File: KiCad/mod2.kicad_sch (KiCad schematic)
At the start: 49 parts, among them M3 Fan_4pin, M4 Fan_4pin, U2 ZD25Q64BSIGT

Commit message: Copy modules 2 and 3, remove unnecessary pages
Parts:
- removed D6: B0520W, Diode_SMD:D_SOD-123, symbol Device:D_Schottky
- removed D7, D8: LED, LED_SMD:LED_0603_1608Metric, symbol Device:LED
- removed R40, R41: 10k, Resistor_SMD:R_0402_1005Metric, symbol Device:R_Small
- removed U2: ZD25Q64BSIGT, Package_SO:SOIC-8_5.3x5.3mm_P1.27mm, symbol Memory_Flash:W25Q128JVS
- added C21, C22, C23, C24, C25, C26: 100nF, Capacitor_SMD:C_0402_1005Metric, symbol Device:C_Small
- added C27, C28, C29, C30, C31, C32, C33, C366, C367: 220nF, Capacitor_SMD:C_0402_1005Metric, symbol Device:C_Small
- added C368, C372, C373, C376: 100nF/50V, Capacitor_SMD:C_0402_1005Metric, symbol Device:C
- added C369: 10uF/10V, Capacitor_SMD:C_0603_1608Metric, symbol Device:C
- added C370, C378: 27pF, Capacitor_SMD:C_0402_1005Metric, symbol Device:C_Small
- added C371: 390pF, Capacitor_SMD:C_0402_1005Metric, symbol Device:C
- added C374, C375: 100uF/25V, Capacitor_SMD:CP_Elec_6.3x7.7, symbol Device:C_Polarized
- added C377: 560uF/25V, Capacitor_SMD:CP_Elec_6.3x7.7, symbol Device:C_Polarized
- added C379: 100pF, Capacitor_SMD:C_0402_1005Metric, symbol Device:C_Small
- added D4, D7: B0520W, Diode_SMD:D_SOD-123, symbol Device:D_Schottky
- added D6: LED, LED_SMD:LED_0603_1608Metric, symbol Device:LED
- added J25: RJE361882415, RJE361882145:AMPHENOL_RJE361882415, symbol Custom:1xRJ45+2xUSB3
- added J28: SFF-8654-8i, EasyEDA2KiCAD:CONN-SMD_HBH2-74AT-1-UHR, symbol Custom:SFF-8654-8i
- added J29: Bus_PCI_Express_x4, EasyEDA2KiCAD:PCIE-TH_AAA-PCI-161-K03, symbol Connector:Bus_PCI_Express_x4
- added Q8: 2N7002, Package_TO_SOT_SMD:SOT-23, symbol Transistor_FET:Q_NMOS_GSD
- added R10, R240, R246, R247: 4.7k, Resistor_SMD:R_0402_1005Metric, symbol Device:R_Small
- added R11: 1k, Resistor_SMD:R_0805_2012Metric, symbol Device:R_Small
- added R241: 15k, Resistor_SMD:R_0402_1005Metric, symbol Device:R_Small
- added R242, R243, R244, R245: 75R, Resistor_SMD:R_0402_1005Metric, symbol Device:R_Small
- added R248: 2.49k, Resistor_SMD:R_0402_1005Metric, symbol Device:R_Small
- added R249, R251, R252: 100k, Resistor_SMD:R_0402_1005Metric, symbol Device:R_Small
- added R250: 10k, Resistor_SMD:R_0402_1005Metric, symbol Device:R_Small
- added TR7: QG2439S, Custom:QG2439S, symbol Transformer:30F-51NL
- added U1, U2, U54, U55, U56, U57, U59, U60: H5VU25U, Package_DFN_QFN:Diodes_UDFN-10_1.0x2.5mm_P0.5mm, symbol Power_Protection:D3V3XA4B10LP
- added U58: RTL8125BG-CG, Package_DFN_QFN:QFN-48-1EP_6x6mm_P0.4mm_EP4.2x4.2mm, symbol Custom:RTL8125BG-CG
- added Y8: 25MHz, Crystal:Crystal_SMD_3225-4Pin_3.2x2.5mm, symbol Device:Crystal_GND24
- C34, C35, C36, C56: value 100nF -> 220nF
- C37: value 100nF -> 1uF
- C38: value 100nF -> 2.2uF
- C39: value 100nF -> 10uF
- C40, C42, C54: value 220nF -> 10uF
- C41, C44, C45: value 220nF -> 2.2uF
- C46: value 10nF -> 220nF
- C47, C48, C50, C53: value 10nF -> 2.2uF
- C49, C51: value 10nF -> 100nF
- C52: value 10nF -> 1uF
- R27: value 4.7k -> 22k
- R28: value 4.7k -> 100R
- R29: value 22k -> 4.7k
- R32: value 100R -> 22k
- R33: value 22k -> 10k
- R34: value 1k -> 2.2k; footprint Resistor_SMD:R_0805_2012Metric -> Resistor_SMD:R_0402_1005Metric
- R35: value 2.2k -> 510R
- R36, R37: value 10k -> 100R
- R38: value 2.2k -> 100R
- R39: value 100k -> 100R
- R42: value 100k -> 510R
- R43: value 10k -> 1k
- R44: value 100k -> 4.7k
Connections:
- net FUSB.SS_Tx1+ is gone; now on net +0V95: C38.1
- net FUSB.SS_Tx1- is gone; now on net GND: C39.1
- net M2_EKEY.Tx0+ is gone; now on net +0V95: C40.1
- net M2_EKEY.Tx0- is gone; now on net GND: C41.1
- net NVME.Tx0+ is gone; now on net +0V95: C42.1
- net NVME.Tx1+ is gone; now on net GND: C44.1
- net NVME.Tx1- is gone; now on net +0V95: C45.1
- net RUSB.SS_Tx1- is gone; now on net GND: C37.1
- net SATA1.Rx+ is gone; now on net +0V95: C48.1
- net SATA1.Rx- is gone; now on net GND: C49.1
- net SATA1.Tx- is gone; now on net GND: C47.1
- net SATA2.Rx+ is gone; now on net +0V95: C52.1
- net SATA2.Rx- is gone; now on net GND: C53.1
- net SATA2.Tx+ is gone; now on net +0V95: C50.1
- net SATA2.Tx- is gone; now on net GND: C51.1
- net UART_RX is gone; now on an unnamed net: A2.137 (UART0_RXD)
- net +12V: now also D5.1 (K), R29.1, C24.1, C372.1, C373.1, C374.1, C375.1, J29.A2 (+12V), J29.A3 (+12V), J29.B1 (+12V), J29.B2 (+12V), J29.B3 (+12V); no longer C35.1, R28.1
- net +3V3: now also R34.1, R43.1, R44.1, C376.1, C377.1, J29.A10 (+3.3V), J29.A9 (+3.3V), J29.B8 (+3.3V), R250.2; no longer C56.1, R35.1, R38.2
- net +5V: now also C21.1, D4.1 (K), J25.U1 (VBUS), J25.U10 (VBUS), R10.1; no longer C34.1, D5.1 (K), R27.1
- net +BATT: now also R11.1; no longer R34.1
- net GND: now also C38.2, C40.2, C42.2, C45.2, C48.2, C50.2, C52.2, C54.2, R32.2, C21.2, C24.2, C368.1, C369.1, C370.1, C371.1, C372.2, C373.2, C374.2, C375.2, C376.2, C377.2, C378.1, C379.2, J25.SH, J25.U13 (GND), J25.U16 (DRAIN), J25.U4 (GND), J25.U7 (DRAIN), J28.A1 (GND), J28.A10 (GND), J28.A13 (GND), J28.A16 (GND), J28.A19 (GND), J28.A22 (GND), J28.A25 (GND), J28.A28 (GND), J28.A31 (GND), J28.A34 (GND), J28.A37 (GND), J28.A4 (GND), J28.A7 (GND), J28.B1 (GND), J28.B10 (GND), J28.B12 (CPRSNTA#), J28.B13 (GND), J28.B16 (GND), J28.B19 (GND), J28.B22 (GND), J28.B25 (GND), J28.B28 (GND), J28.B30 (CPRSNTB#), J28.B31 (GND), J28.B34 (GND), J28.B37 (GND), J28.B4 (GND), J28.B7 (GND), J28.SH, J28.SH, J29.A1 (~{PRSNT1}), J29.A12 (GND), J29.A15 (GND), J29.A18 (GND), J29.A20 (GND), J29.A23 (GND), J29.A24 (GND), J29.A27 (GND), J29.A28 (GND), J29.A31 (GND), J29.A4 (GND), J29.B13 (GND), J29.B16 (GND), J29.B17 (~{PRSNT2}), J29.B18 (GND), J29.B21 (GND), J29.B22 (GND), J29.B25 (GND), J29.B26 (GND), J29.B29 (GND), J29.B31 (~{PRSNT2}), J29.B32 (GND), J29.B4 (GND), J29.B7 (GND), Q8.2 (S), R241.2, R248.2, R249.1, R251.1, R252.1, U1.3 (VSS), U1.8 (VSS), U2.3 (VSS), U2.8 (VSS), U54.3 (VSS), U54.8 (VSS), U55.3 (VSS), U55.8 (VSS), U56.3 (VSS), U56.8 (VSS), U57.3 (VSS), U57.8 (VSS), U58.40 (GND), U58.49 (GND), U59.3 (VSS), U59.8 (VSS), U60.3 (VSS), U60.8 (VSS), Y8.2, Y8.4; no longer C34.2, C35.2, C56.2, R36.2, R37.2, R39.1, R42.1, R43.2, R44.1
- net at A2.55 (HSIO11_TX+): now also C43.2; no longer C50.2
- net at A2.45 (HSIO9_TX-): now also C34.2; no longer C45.2
- net at C55.2: now also A2.61 (HSIO6_TX+); no longer A2.63 (HSIO6_TX-)
- net PCIEX4_RX2+: now reaches A2.52 (HSIO10_RX+)
- net PCIEX4_RX2+: now also J29.A25 (PERp2); no longer C48.2
- net CASE_FAN_PWM: now reaches R31.1
- net CASE_FAN_PWM: now also A2.6 (FAN2_PWM); no longer A2.2 (FAN1_PWM)
- net at M3.4 (PWM): now also R28.2; no longer R31.2
- net at R36.1: no longer A2.100 (~{CLKREQ3})
- net at A2.102 (~{CLKREQ4}): now also R33.1; no longer R37.1
- net SMB_DATA: now reaches A2.106 (SMB_CLK)
- net SMB_DATA: now also J28.B27 (2W-DATAB), J28.B9 (2W-DATAA), J29.B6 (SMDAT)
- net SMB_CLK: now reaches A2.108 (SMB_DATA)
- net SMB_CLK: now also J28.B26 (2W-CLKB), J28.B8 (2W-CLKA), J29.B5 (SMCLK)
- net at A2.115 (VBAT): now also R11.2; no longer R34.2
- net at A2.13 (HSIO0_TX+): now also C22.2; no longer C36.2
- net at A2.133 (~{BIOS_SEL}): now also R250.1; no longer R43.1
- net at A2.141 (UART1_RXD): now also R38.1
- net at A2.143 (UART1_TXD): now also R39.1
- net at A2.15 (HSIO0_TX-): now also C23.2; no longer C37.2
- net at A2.183 (DDIB_HPD): now also R252.2; no longer R39.2
- net at A2.185 (TCP1_HPD): now also R251.2; no longer R44.2
- net at A2.187 (TCP0_HPD): now also R249.2; no longer R42.2
- net at A2.19 (HSIO1_TX+): now also C25.2; no longer C38.2
- net at A2.21 (HSIO1_TX-): now also C26.2; no longer C39.2
- net at A2.25 (HSIO2_TX+): now also C27.2; no longer C40.2
- net at A2.27 (HSIO2_TX-): now also C28.2; no longer C41.2
- net at A2.31 (HSIO3_TX+): now also C29.2
- net at A2.33 (HSIO3_TX-): now also C30.2
- net NVME1_RX+: now reaches A2.34 (HSIO3_RX+)
- net NVME1_RX+: now also J28.A20 (PERp4)
- net NVME1_RX-: now reaches A2.36 (HSIO3_RX-)
- net NVME1_RX-: now also J28.A21 (PERn4)
- net at A2.37 (HSIO8_TX+): now also C31.2; no longer C42.2
- net at A2.39 (HSIO8_TX-): now also C32.2; no longer C43.2
- net CPU_FAN_TAC: now reaches A2.4 (FAN1_TAC)
- net CPU_FAN_TAC: now also R27.1; no longer R29.1
- net at A2.43 (HSIO9_TX+): now also C33.2; no longer C44.2
- net at A2.49 (HSIO10_TX+): now also C35.2; no longer C46.2
- net POWER_S0: now reaches A2.5 (SLS_S0)
- net POWER_S0: now also R43.2, Q8.1 (G), R241.1, U58.1 (~{ISOLATEB})
- net at A2.51 (HSIO10_TX-): now also C36.2; no longer C47.2
- net +3V3SB: now reaches C49.2
- net +3V3SB: now also C37.2, C39.2, C41.2, C44.2, C47.2, C51.2, C53.2, R35.2, R42.2, C368.2, C369.2, J29.B10 (3.3Vaux), R240.1, R246.2, R247.2, U58.15 (AVDD33), U58.19 (AVDD33), U58.29 (DVDD33), U58.33 (AVDD33), U58.34 (AVDD33_XTAL), U58.43 (EVDD33), U58.46 (DVDD33); no longer A2.54 (HSIO10_RX-)
- net at A2.57 (HSIO11_TX-): now also C46.2; no longer C51.2
- net PCIEX4_RX3+: now reaches A2.58 (HSIO11_RX+)
- net PCIEX4_RX3+: now also J29.A29 (PERp3); no longer C52.2
- net CASE_FAN_TAC: now reaches R32.1
- net CASE_FAN_TAC: now also A2.8 (FAN2_TAC), R30.1; no longer A2.6 (FAN2_PWM)
- net PCIEX4_RX3-: now reaches A2.60 (HSIO11_RX-)
- net PCIEX4_RX3-: now also J29.A30 (PERn3); no longer C53.2
- net ETH_REFCLK+: now reaches A2.88 (REFCLK3+)
- net ETH_REFCLK+: now also U58.44 (REFCLK+)
- net ETH_REFCLK-: now reaches A2.90 (REFCLK3-)
- net ETH_REFCLK-: now also U58.45 (REFCLK-)
- net at M3.3 (Tacho), R27.2: now also D4.2 (A), R10.2; no longer D5.2 (A), R29.2
- net at M4.3 (Tacho), R30.2: now also D5.2 (A), R29.2; no longer R28.2
- net at M4.4 (PWM): now also R31.2; no longer R32.2
- net ETH.REFCLK+ renamed NVME0_REFCLK+
- net NVME0_REFCLK+: now also J28.A11 (REFCLKA+)
- net ETH.REFCLK- renamed NVME0_REFCLK-
- net NVME0_REFCLK-: now also J28.A12 (REFCLKA-)
- net ETH.Rx0+ renamed ETH_RX+
- net ETH_RX+: now also C366.1
- net ETH.Rx0- renamed ETH_RX-
- net ETH_RX-: now also C367.1
- net ETH.SMBCLK: no longer names the net of A2.147 (SML1_CLK)
- net ETH.SMBDAT: no longer names the net of A2.145 (SML1_DATA)
- net ETH.Tx0+ renamed +0V95
- net +0V95: now also U58.11 (AVDD09), U58.16 (AVDD09), U58.22 (AVDD09), U58.28 (DVDD09), U58.37 (EVDD09), U58.47 (DVDD09), U58.8 (DVDD09)
- net ETH.Tx0- renamed ETH_TX+
- net ETH_TX+: now also U58.41 (Rx+)
- net ETH.~{PLTRST} renamed ~{PCIE_RST}
- net ~{PCIE_RST}: now also J28.B11 (PERSTA#), J28.B29 (PERSTB#), J29.A11 (~{PERST}), U58.36 (~{PERRST})
- net ETH.~{WAKE} renamed ~{PCIE_WAKE}
- net ~{PCIE_WAKE}: now also J28.A27 (CWAKEB#), J28.A9 (CWAKEA#), J29.B11 (~{WAKE}), R240.2, U58.2 (LANWAKEB)
- net FUSB.D+ renamed RUSB1_D+
- net RUSB1_D+: now also J25.U11 (D-), U1.4, U1.7 (NC)
- net FUSB.D- renamed RUSB1_D-
- net RUSB1_D-: now also J25.U12 (D+), U1.5, U1.6 (NC)
- net FUSB.SS_Rx1+ renamed RUSB1_SSRX+
- net RUSB1_SSRX+: now also J25.U14 (SSRX-), U54.1, U54.10 (NC)
- net FUSB.SS_Rx1- renamed RUSB1_SSRX-
- net RUSB1_SSRX-: now also J25.U15 (SSRX+), U54.2, U54.9 (NC)
- net M2_EKEY.REFCLK+ renamed PCIEX4_REFCLK+
- net PCIEX4_REFCLK+: now also J29.A13 (REFCLK+)
- net M2_EKEY.REFCLK- renamed PCIEX4_REFCLK-
- net PCIEX4_REFCLK-: now also J29.A14 (REFCLK-)
- net M2_EKEY.Rx0+ renamed NVME0_RX+
- net NVME0_RX+: now also J28.A2 (PERp0)
- net M2_EKEY.Rx0- renamed NVME0_RX-
- net NVME0_RX-: now also J28.A3 (PERn0)
- net M2_EKEY.SUSCLK: no longer names the net of A2.131 (SUSCLK)
- net M2_EKEY.USB-D+: no longer names the net of A2.81 (USB2_P3+)
- net M2_EKEY.USB-D-: no longer names the net of A2.79 (USB2_P3-)
- net NVME.REFCLK+ renamed NVME1_REFCLK+
- net NVME1_REFCLK+: now also J28.A29 (REFCLKB+)
- net NVME.REFCLK- renamed NVME1_REFCLK-
- net NVME1_REFCLK-: now also J28.A30 (REFCLKB-)
- net NVME.Rx0+ renamed PCIEX4_RX0+
- net PCIEX4_RX0+: now also J29.A16 (PERp0)
- net NVME.Rx0- renamed PCIEX4_RX0-
- net PCIEX4_RX0-: now also J29.A17 (PERn0)
- net NVME.Rx1+ renamed PCIEX4_RX1+
- net PCIEX4_RX1+: now also J29.A21 (PERp1)
- net NVME.Rx1- renamed PCIEX4_RX1-
- net PCIEX4_RX1-: now also J29.A22 (PERn1)
- net NVME.Tx0- renamed PCIEX4_TX3+
- net PCIEX4_TX3+: now also J29.B27 (PETp3)
- net RUSB.D+ renamed RUSB0_D+
- net RUSB0_D+: now also J25.U2 (D-), U1.1, U1.10 (NC)
- net RUSB.D- renamed RUSB0_D-
- net RUSB0_D-: now also J25.U3 (D+), U1.2, U1.9 (NC)
- net RUSB.SS_Rx1+ renamed RUSB0_SSRX+
- net RUSB0_SSRX+: now also J25.U5 (SSRX-), U2.1, U2.10 (NC)
- net RUSB.SS_Rx1- renamed RUSB0_SSRX-
- net RUSB0_SSRX-: now also J25.U6 (SSRX+), U2.2, U2.9 (NC)
- net RUSB.SS_Tx1+ renamed PCIEX4_TX2-
- net PCIEX4_TX2-: now also J29.B24 (PETn2)
- net SATA1.Tx+ renamed PCIEX4_TX3-
- net PCIEX4_TX3-: now also J29.B28 (PETn3)
- net UART_TX: no longer names the net of A2.139 (UART0_TXD)
- net UART_TX: now also R37.1
- new net: C370.2, U58.10 (CKXTAL1), Y8.1
- new net: A2.63 (HSIO6_TX-), C56.2
- new net: C379.1, R242.2, R243.2, R244.2, R245.2
- new net: R246.1, U58.3 (GPI)
- new net: C367.2, U58.39 (Tx-)
- new net: R243.1, TR7.21 (CT)
- new net: R248.1, U58.12 (RSET)
- new net: C378.2, U58.9 (CKXTAL2), Y8.3
- new net: R245.1, TR7.15 (CT)
- new net: C366.2, U58.38 (Tx+)
- new net: U58.4 (NC), U58.5 (NC), U58.7 (NC)
- new net: D7.2 (A), U58.6 (POW_EXT_SWR)
- new net: D6.1 (K), Q8.3 (D)
- new net: D6.2 (A), R34.2
- new net: J25.1, TR7.13 (MX4-)
- new net: J25.2, TR7.14 (MX4+)
- new net: J25.3, TR7.16 (MX3-)
- new net: J25.6, TR7.17 (MX3+)
- new net: R244.1, TR7.18 (CT)
- new net: J25.4, TR7.19 (MX2-)
- new net: J25.5, TR7.20 (MX2+)
- new net: J25.7, TR7.22 (MX1-)
- new net: J25.8, TR7.23 (MX1+)
- new net: R242.1, TR7.24 (CT)
- new net: J25.D1, R42.1
- new net: J25.D3, R35.1
- new net 0V95_ENABLE: D7.1 (K)
- new net BMC_UART_RX: R36.2
- new net BMC_UART_TX: R37.2
- new net CPU_FAN_PWM: A2.2 (FAN1_PWM), R28.1
- new net ETH_LED0: J25.D4, U58.30 (EEDI/SDA)
- new net ETH_LED1: J25.D2, R247.1, U58.27 (EESK)
- new net ETH_TX-: C56.1, U58.42 (Rx-)
- new net HDMI_CK+: U59.4, U59.7 (NC)
- new net HDMI_CK-: U59.5, U59.6 (NC)
- new net HDMI_D0+: U59.1, U59.10 (NC)
- new net HDMI_D0-: U59.2, U59.9 (NC)
- new net HDMI_D1+: U57.4, U57.7 (NC)
- new net HDMI_D1-: U57.5, U57.6 (NC)
- new net HDMI_D2+: U57.1, U57.10 (NC)
- new net HDMI_D2-: U57.2, U57.9 (NC)
- new net HDMI_HPDO: U60.5, U60.6 (NC)
- new net HDMI_SCLO: U60.1, U60.10 (NC)
- new net HDMI_SDAO: U60.2, U60.9 (NC)
- new net MDI0+: TR7.12 (TD4-), U55.1, U55.10 (NC), U58.13 (MDI[0]+)
- new net MDI0-: TR7.11 (TD4+), U55.2, U55.9 (NC), U58.14 (MDI[0]-)
- new net MDI1+: TR7.9 (TD3-), U55.4, U55.7 (NC), U58.17 (MDI[1]+)
- new net MDI1-: TR7.8 (TD3+), U55.5, U55.6 (NC), U58.18 (MDI[1]-)
- new net MDI2+: TR7.6 (TD2-), U56.1, U56.10 (NC), U58.20 (MDI[2]+)
- new net MDI2-: TR7.5 (TD2+), U56.2, U56.9 (NC), U58.21 (MDI[2]-)
- new net MDI3+: TR7.3 (TD1-), U56.4, U56.7 (NC), U58.23 (MDI[3]+)
- new net MDI3-: C371.2, TR7.1 (CT), TR7.10 (CT), TR7.2 (TD1+), TR7.4 (CT), TR7.7 (CT), U56.5, U56.6 (NC), U58.24 (MDI[3]-)
- new net NVME0_TX+: C27.1, J28.B2 (PETp0)
- new net NVME0_TX-: C28.1, J28.B3 (PETn0)
- new net NVME1_TX+: C29.1, J28.B20 (PETp4)
- new net NVME1_TX-: C30.1, J28.B21 (PETn4)
- new net PCIEX4_RX2-: A2.54 (HSIO10_RX-), J29.A26 (PERn2)
- new net PCIEX4_TX0+: C31.1, J29.B14 (PETp0)
- new net PCIEX4_TX0-: C32.1, J29.B15 (PETn0)
- new net PCIEX4_TX1+: C33.1, J29.B19 (PETp1)
- new net PCIEX4_TX1-: C34.1, J29.B20 (PETn1)
- new net PCIEX4_TX2+: C35.1, J29.B23 (PETp2)
- new net RUSB0_SSTX+: C22.1, J25.U8 (SSTX-), U2.4, U2.7 (NC)
- new net RUSB0_SSTX-: C23.1, J25.U9 (SSTX+), U2.5, U2.6 (NC)
- new net RUSB1_SSTX+: C25.1, J25.U17 (SSTX-), U54.4, U54.7 (NC)
- new net RUSB1_SSTX-: C26.1, J25.U18 (SSTX+), U54.5, U54.6 (NC)
- new net SLOT1_UART_RX: R38.2
- new net SLOT1_UART_TX: R39.2
- new net ~{ETH_CLKREQ}: A2.100 (~{CLKREQ3}), R44.2, U58.48 (CLKREQB)
- no-connect marks 111 -> 154
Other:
- note added: "2.5G Ethernet"
- note added: "2x U.2 NVME"
- note added: "Fans"
- note added: "LattePanda Mu Module"
- note added: "PCIe x4 Slot"
- note added: "Power LED"
- note added: "USB 3"

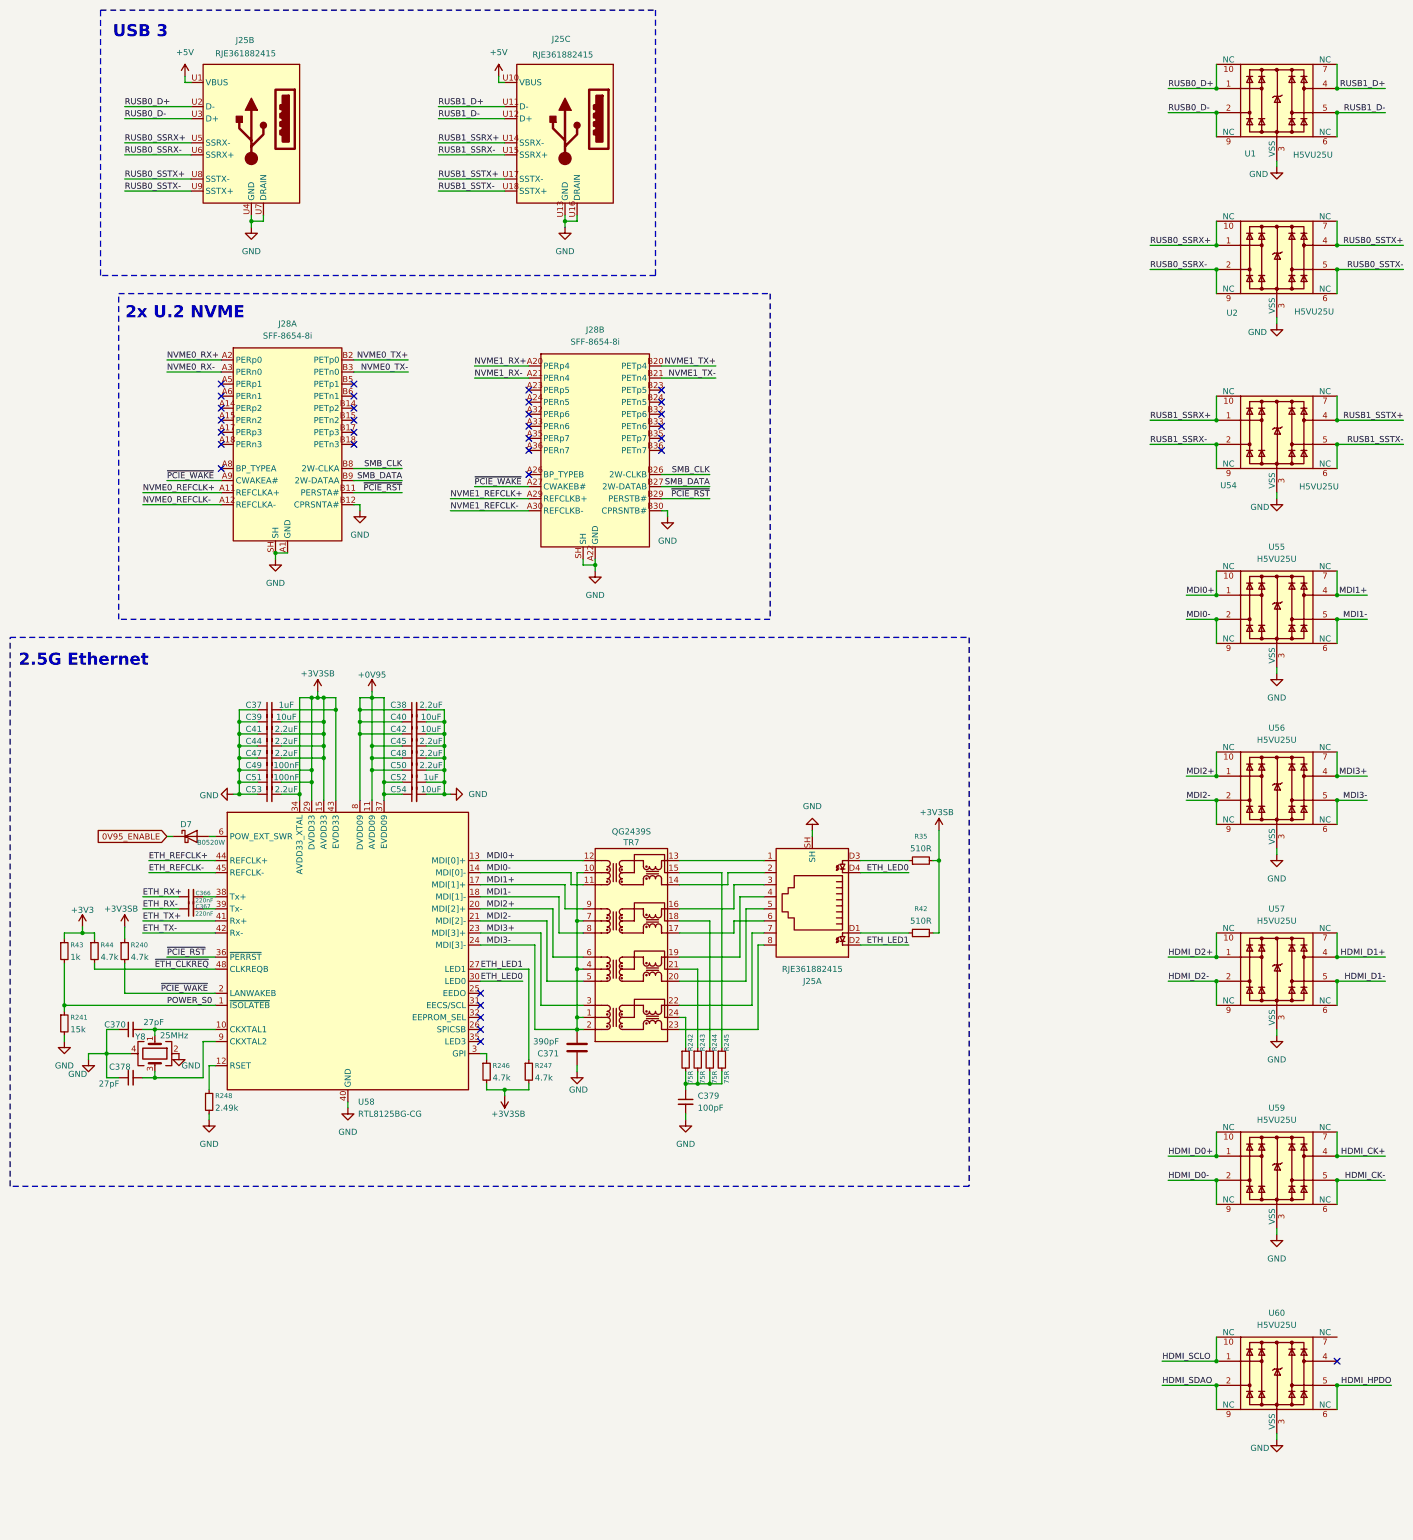
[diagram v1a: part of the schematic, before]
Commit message: Add 0.95V supply, Fix connectors
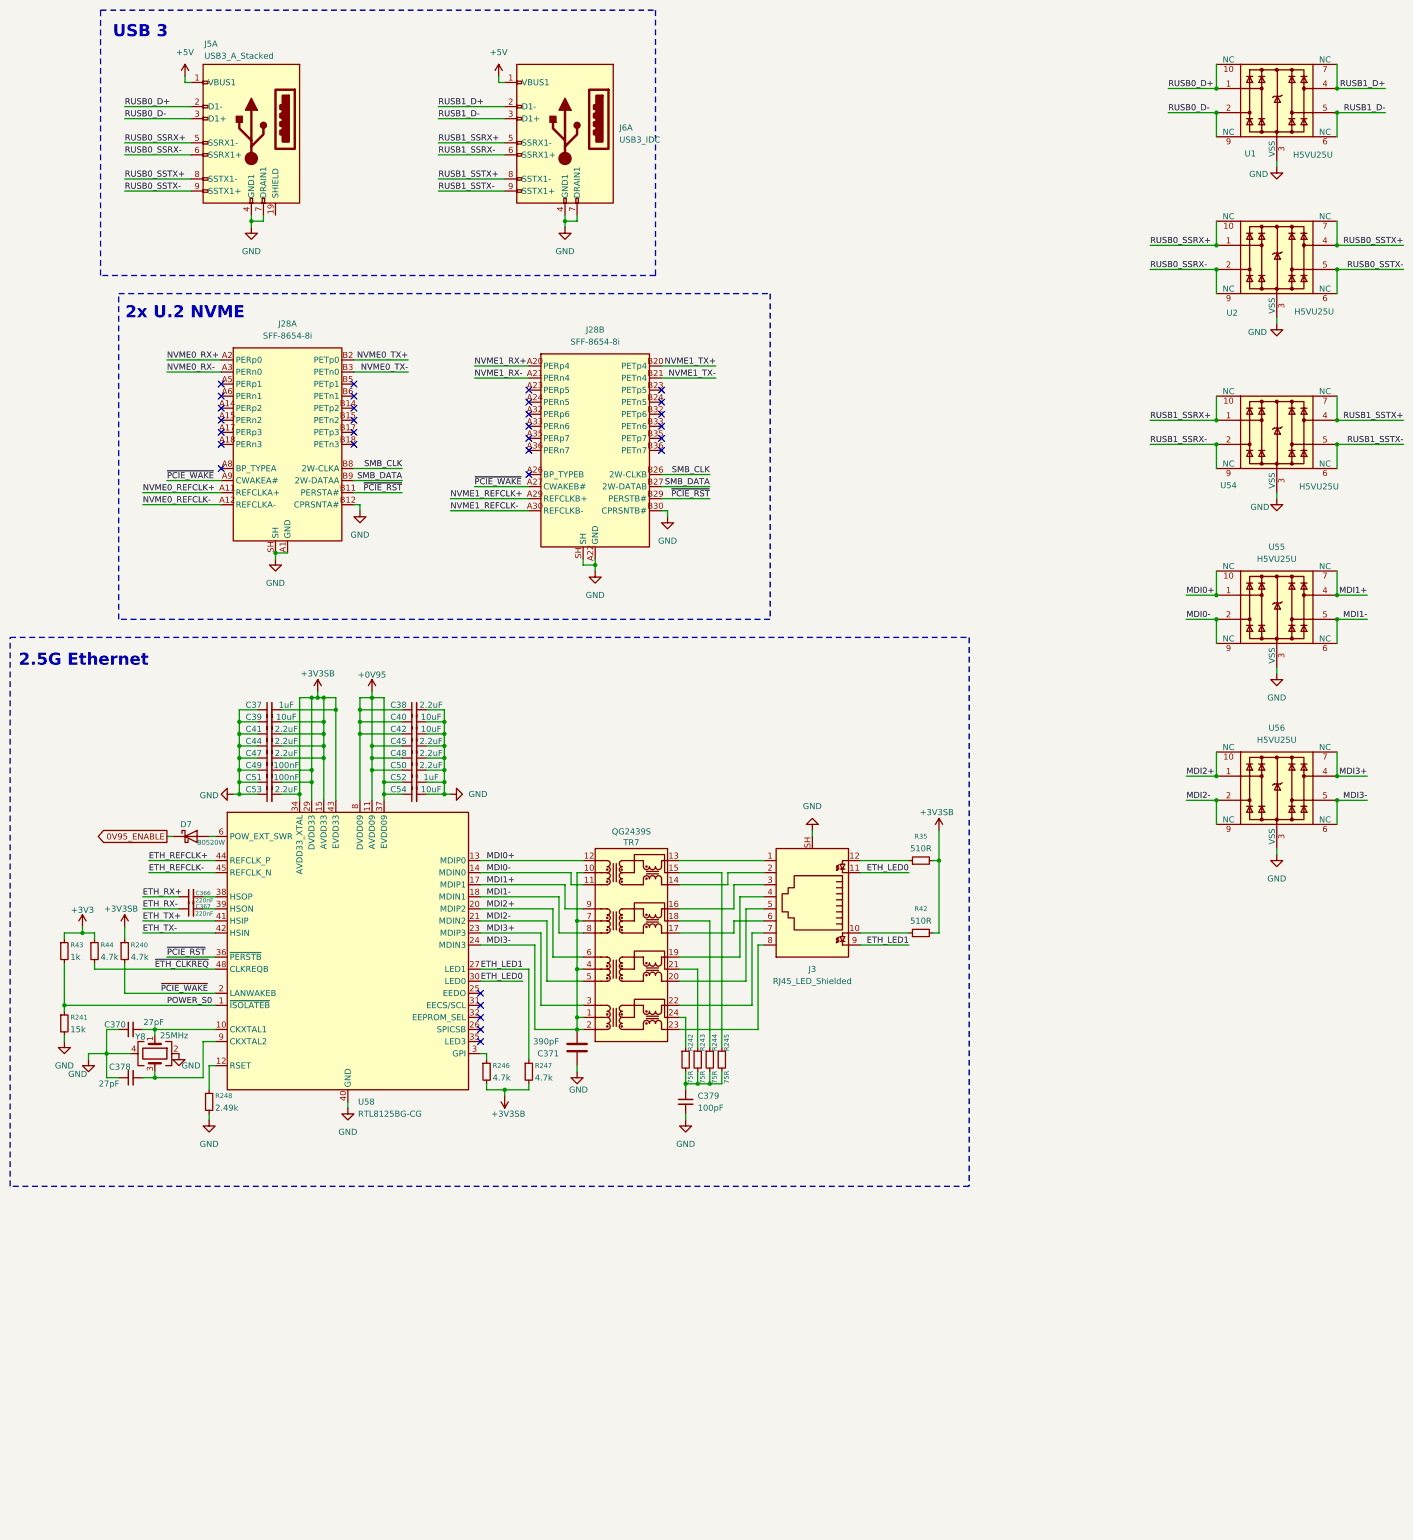
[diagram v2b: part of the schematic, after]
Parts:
- removed J25: RJE361882415, RJE361882145:AMPHENOL_RJE361882415, symbol Custom:1xRJ45+2xUSB3
- removed U57, U59, U60: H5VU25U, Package_DFN_QFN:Diodes_UDFN-10_1.0x2.5mm_P0.5mm, symbol Power_Protection:D3V3XA4B10LP
- added J3: RJ45_LED_Shielded, Connector_RJ:RJ45_Amphenol_RJHSE538X, symbol Connector:RJ45_LED_Shielded
- added J5: USB3_A_Stacked, EasyEDA2KiCAD:USB-A-TH_HC-USB3.0-L175-2X1-J, symbol Connector:USB3_A_Stacked
- added J6: USB3_IDC, Connector_IDC:IDC-Header_2x10_P2.54mm_Vertical, symbol Custom:USB3_IDC
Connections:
- net +5V: now also J5.1 (VBUS1), J6.1 (VBUS1)
- net ETH_LED0: now also J3.11
- net ETH_LED1: now also J3.9
- net GND: now also J3.SH, J5.4 (GND1), J5.7 (DRAIN1), J6.4 (GND1), J6.7 (DRAIN1)
- net RUSB0_D+: now also J5.2 (D1-)
- net RUSB0_D-: now also J5.3 (D1+)
- net RUSB0_SSRX+: now also J5.5 (SSRX1-)
- net RUSB0_SSRX-: now also J5.6 (SSRX1+)
- net RUSB0_SSTX+: now also J5.8 (SSTX1-)
- net RUSB0_SSTX-: now also J5.9 (SSTX1+)
- net RUSB1_D+: now also J6.2 (D1-)
- net RUSB1_D-: now also J6.3 (D1+)
- net RUSB1_SSRX+: now also J6.5 (SSRX1-)
- net RUSB1_SSRX-: now also J6.6 (SSRX1+)
- net RUSB1_SSTX+: now also J6.8 (SSTX1-)
- net RUSB1_SSTX-: now also J6.9 (SSTX1+)
- net at TR7.13 (MX4-): now also J3.1
- net at TR7.14 (MX4+): now also J3.2
- net at TR7.16 (MX3-): now also J3.3
- net at TR7.17 (MX3+): now also J3.6
- net at TR7.19 (MX2-): now also J3.4
- net at TR7.20 (MX2+): now also J3.5
- net at TR7.22 (MX1-): now also J3.7
- net at TR7.23 (MX1+): now also J3.8
- net at R42.1: now also J3.10
- net at R35.1: now also J3.12
- no-connect marks 154 -> 153
